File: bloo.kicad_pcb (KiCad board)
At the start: 2 copper layers, 90 x 96 mm, 90 parts, among them J5 SWD_Header, M1 M1_Conn_Alt, M2 M2_Conn_Alt, Q0 TEFT4300, Q1 TEFT4300, Q10 Q_NMOS_GSD, Q11 Q_NMOS_GSD, Q12 Q_NMOS_GSD, Q2 TEFT4300, Q3 TEFT4300, Q9 Q_NMOS_GSD, SW1 SW, SW2 SW, SW3 SW, U1 YAAJ_BluePill_SWD_Breakout, U2 L293D, U3 LM1085-5.0, U4 NCP161ASN330T1G, U5 BC832

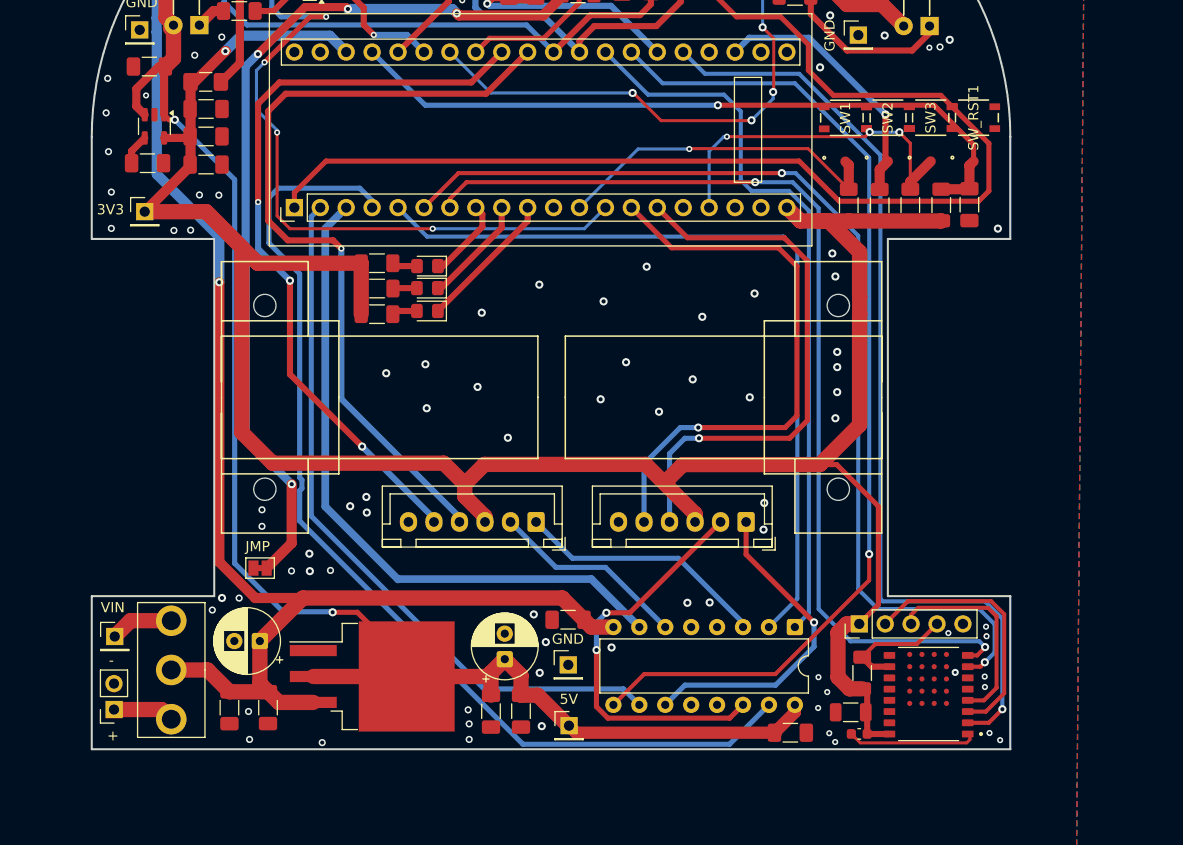
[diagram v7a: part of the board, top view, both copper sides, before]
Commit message: updated pcb from schematics
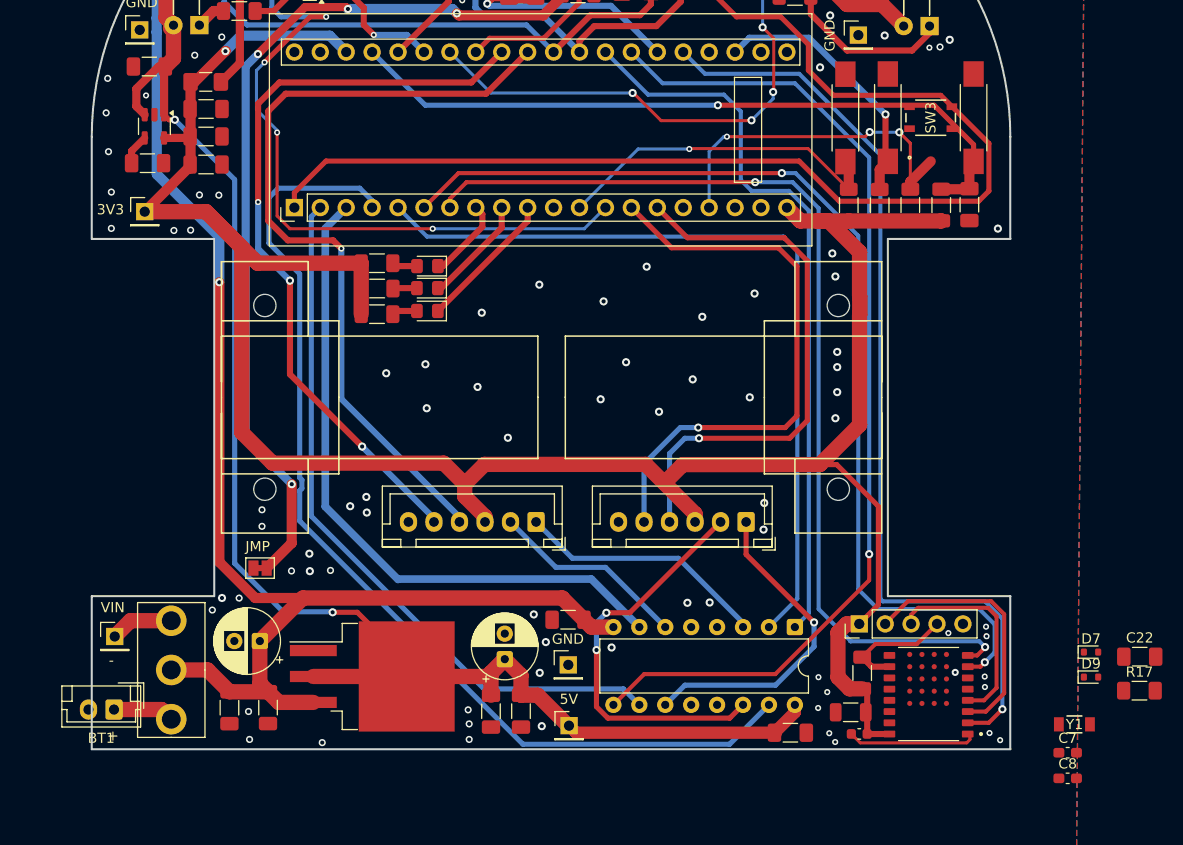
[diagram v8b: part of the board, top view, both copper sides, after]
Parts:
- added C22: 0.1uF, Capacitor_SMD:C_1206_3216Metric_Pad1.33x1.80mm_HandSolder, F.Cu at (312.2, 126.0)
- added C7: 12pF, Capacitor_SMD:C_0603_1608Metric_Pad1.08x0.95mm_HandSolder, F.Cu at (305.1, 135.4)
- added C8: 12pF, Capacitor_SMD:C_0603_1608Metric_Pad1.08x0.95mm_HandSolder, F.Cu at (305.1, 137.9)
- added D7: 1SS389,L3F, Diode_SMD:D_SOD-523, F.Cu at (307.4, 125.6)
- added D9: 1SS389,L3F, Diode_SMD:D_SOD-523, F.Cu at (307.4, 128.0)
- added R17: 47K, Resistor_SMD:R_1206_3216Metric_Pad1.30x1.75mm_HandSolder, F.Cu at (312.1, 129.4)
- added Y1: ABS07-32.768KHZ-T, MM_Library:CAP_ABS07-32.768KHZ-T_ABR, F.Cu at (305.8, 132.7)
- BT1: footprint Connector_PinSocket_2.54mm:PinSocket_1x02_P2.54mm_Vertical -> Connector_JST:JST_EH_B2B-EH-A_1x02_P2.50mm_Vertical
- SW1, SW2, SW_RST1: footprint MM_Library:SW4_SKRPABE010_ALPS -> Button_Switch_SMD:SW_SPST_REED_CT05-XXXX-G1
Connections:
- C19 pad 1: RST -> GND
- C19 pad 2: GND -> RST
- M1 pad 1: M2_OUT_1 -> GND
- M1 pad 2: M2_OUT_2 -> M1_ENC_B
- M1 pad 3: +3V3 -> M1_ENC_A
- M1 pad 4: M2_ENC_A -> +3V3
- M1 pad 5: M2_ENC_B -> M1_OUT_2
- M1 pad 6: GND -> M1_OUT_1
- M2 pad 1: M1_OUT_1 -> GND
- M2 pad 2: M1_OUT_2 -> M2_ENC_B
- M2 pad 3: +3V3 -> M2_ENC_A
- M2 pad 4: M1_ENC_A -> +3V3
- M2 pad 5: M1_ENC_B -> M2_OUT_2
- M2 pad 6: GND -> M2_OUT_1
- R24 pad 2: BUTTON_2 -> BUTTON
- R9 pad 2: BUTTON_3 -> BUTTON_2
- SW2 pad 1: BUTTON_2 -> BUTTON
- SW3 pad 1: BUTTON_3 -> BUTTON_2
- SW_RST1 pad 1: RST -> Net-(D7-K)
- U1 pad 11: unconnected-(U1-PB3-Pad11) -> BLE_SPI_SCK
- U1 pad 12: BUTTON -> BLE_SPI_MISO
- U1 pad 13: EMIT_4 -> BLE_SPI_MOSI
- U1 pad 17: BUTTON_3 -> BUTTON_2
- U1 pad 22: unconnected-(U1-PC13-Pad22) -> EMIT_4
- U1 pad 23: BUTTON_2 -> BUTTON
- U1 pad 24: unconnected-(U1-PC15-Pad24) -> BLE_LED
- U5 pad 11: unconnected-(U5-P00/XL1-Pad11) -> Net-(U5-P00/XL1)
- U5 pad 12: unconnected-(U5-P01/XL2-Pad12) -> Net-(U5-P01/XL2)
- U5 pad 2: BLE_STATE -> unconnected-(U5-P20/LED-Pad2)
- U5 pad A2: unconnected-(U5-P17-PadA2) -> BLE_LED
- U5 pad A5: unconnected-(U5-P08-PadA5) -> BLE_SPI_SCK
- U5 pad C5: unconnected-(U5-P09-PadC5) -> BLE_SPI_MISO
- U5 pad D2: unconnected-(U5-P19-PadD2) -> BLE_STATE
- U5 pad D5: unconnected-(U5-P10-PadD5) -> BLE_SPI_MOSI
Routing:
- net BUTTON_3: track 34.5 -> 0.00 mm, vias 3 -> 0
- net BUTTON: track 33.3 -> 60.1 mm, vias 1 -> 2
- net BUTTON_2: track 26.8 -> 34.5 mm, vias 1 -> 3
